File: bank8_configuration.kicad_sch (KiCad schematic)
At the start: 19 parts, among them IC1 ECP5-BGA256, U7 W25Q32JVSS

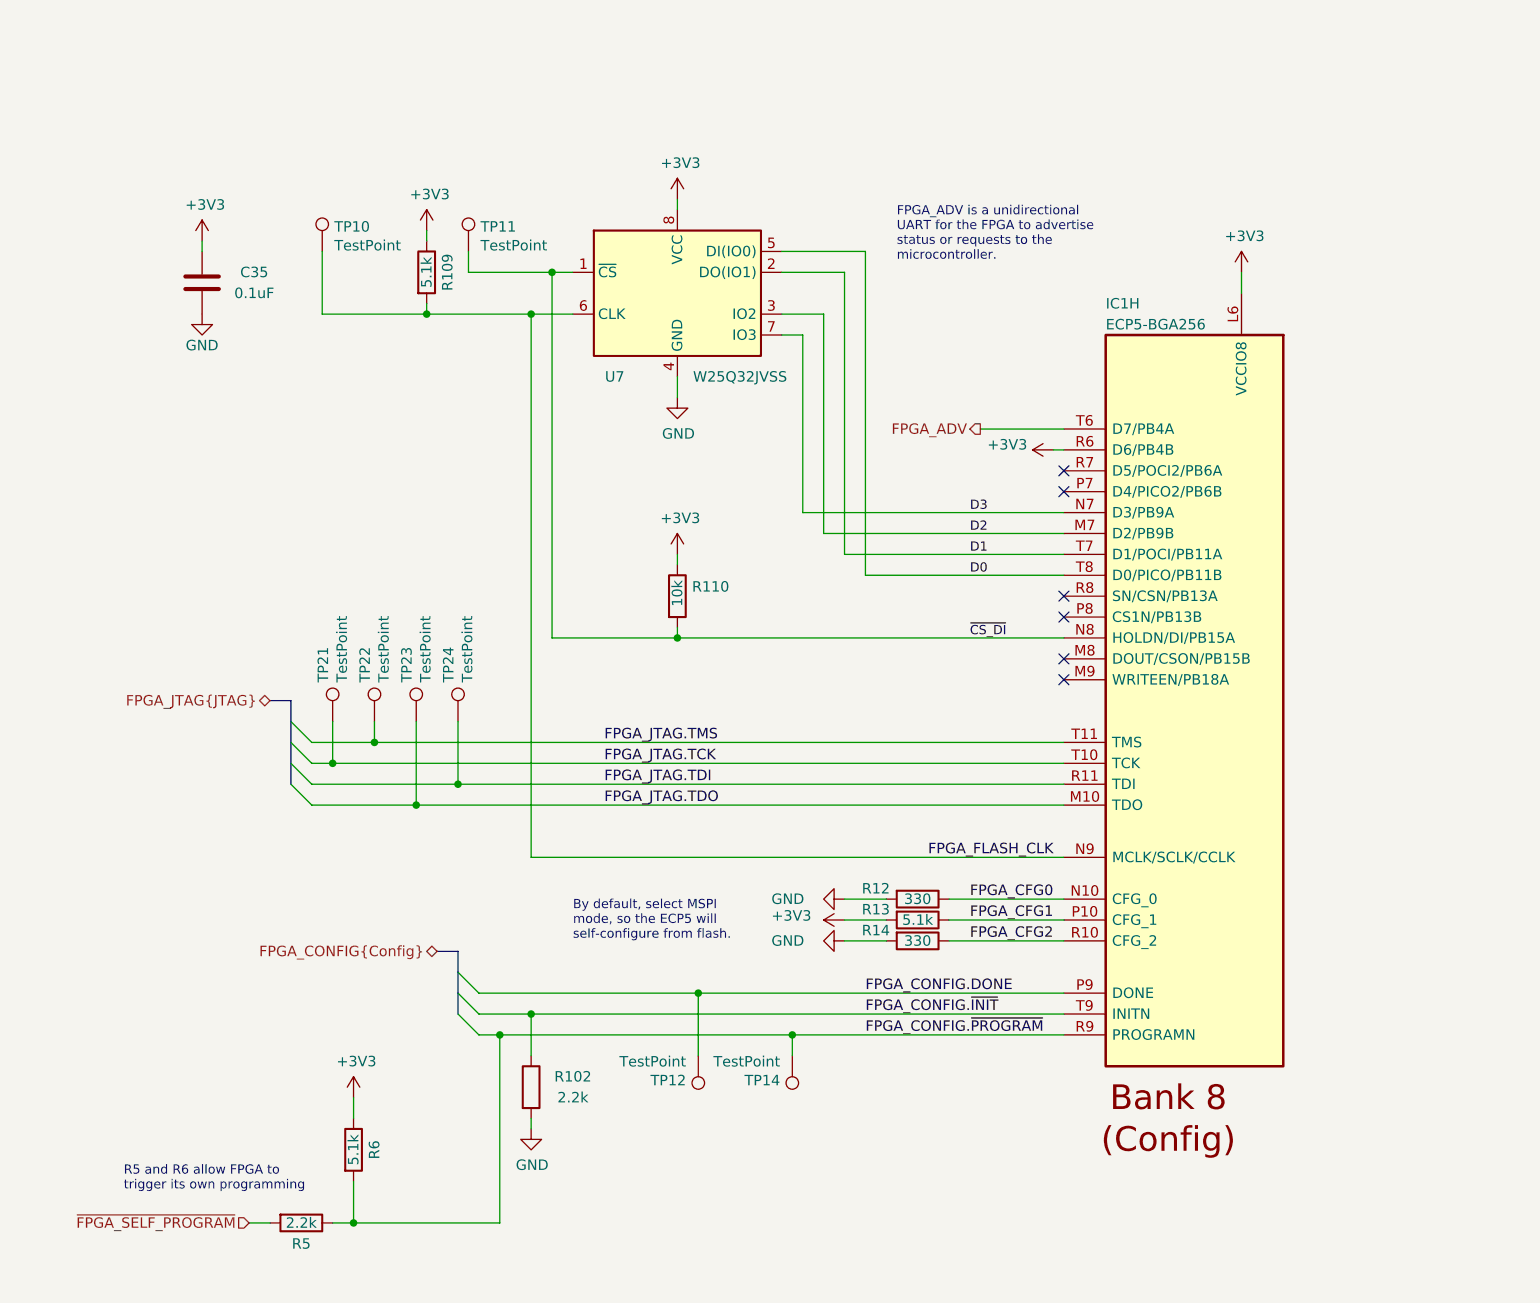
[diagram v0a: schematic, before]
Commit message: Upgrade to KiCad 7
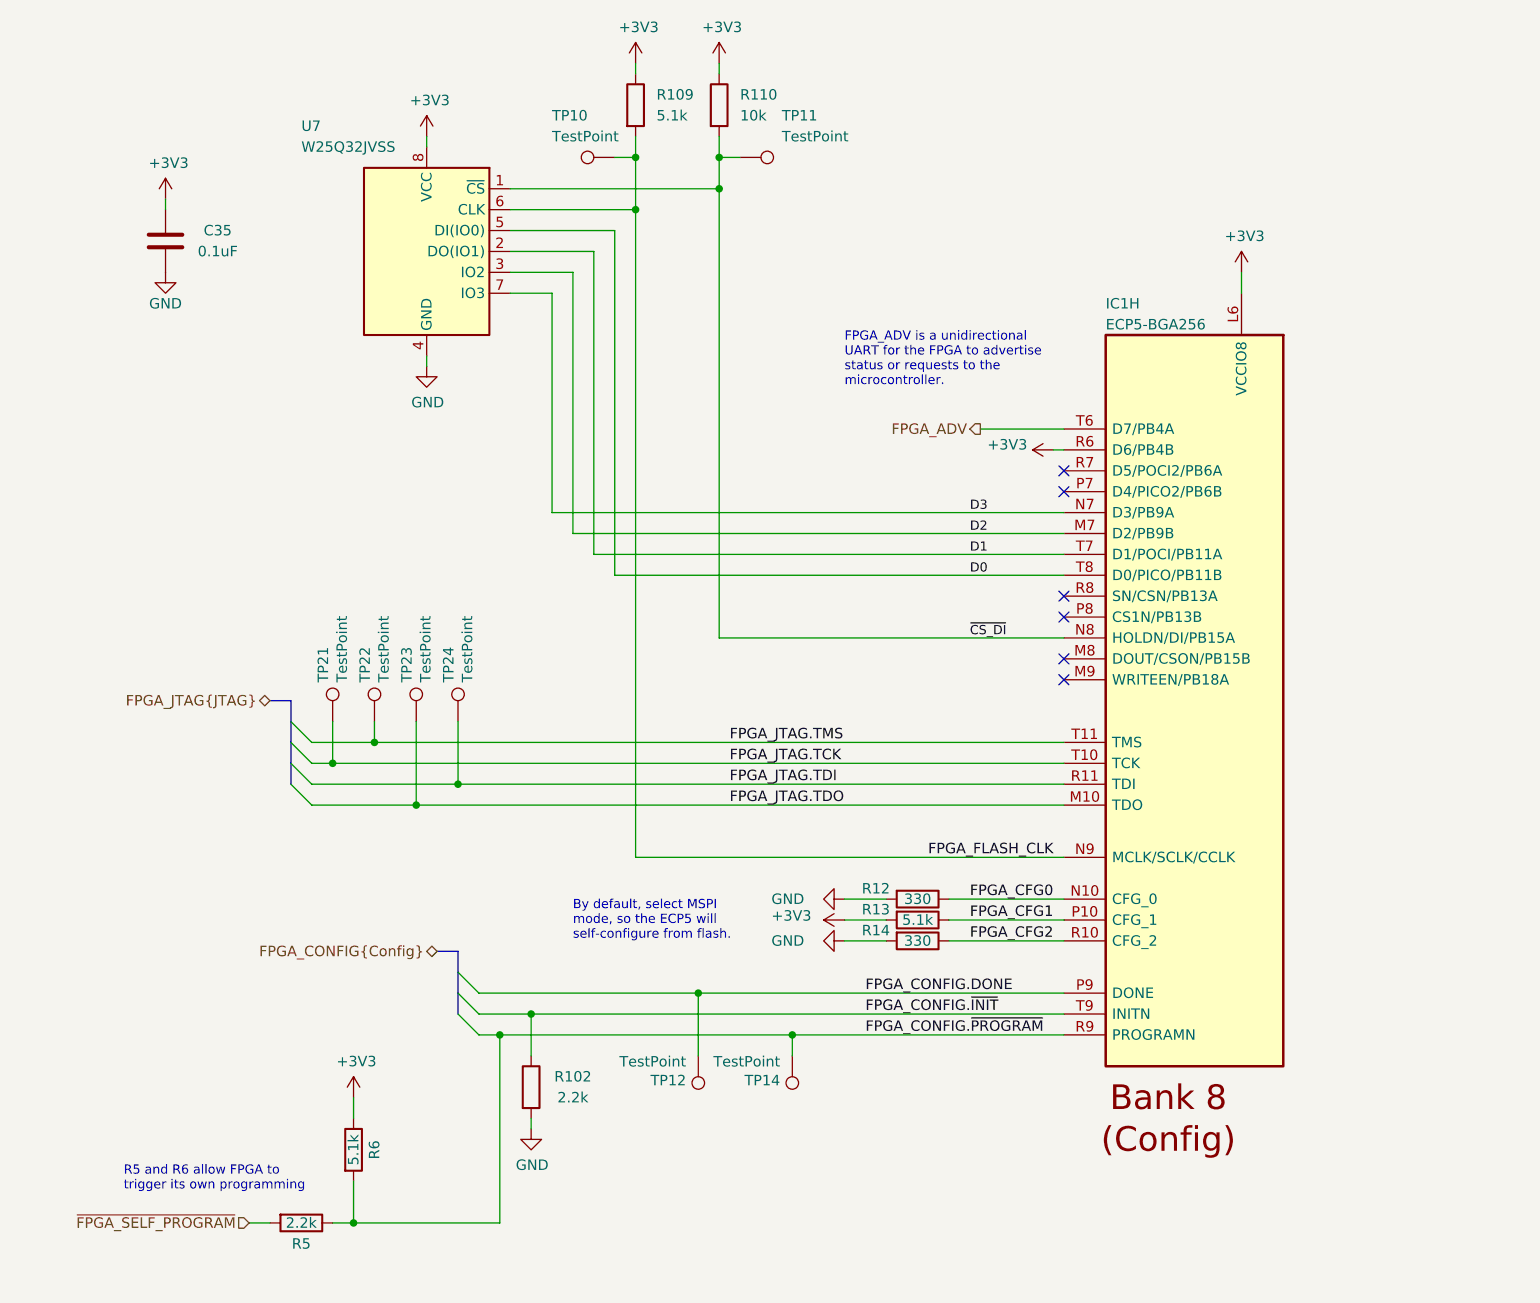
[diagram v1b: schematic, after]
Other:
- moved on the sheet: C35, R109, R110, TP10, TP11, U7

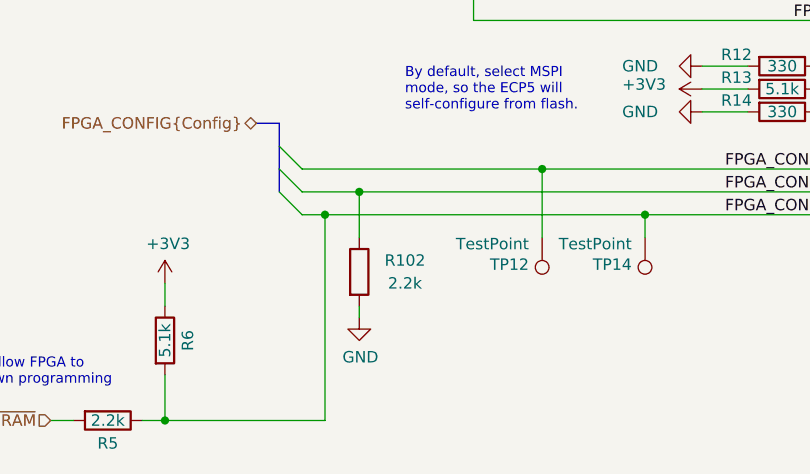
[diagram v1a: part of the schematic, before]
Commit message: Add FPGA_INIT (INITN) series resistor
Fixes #14
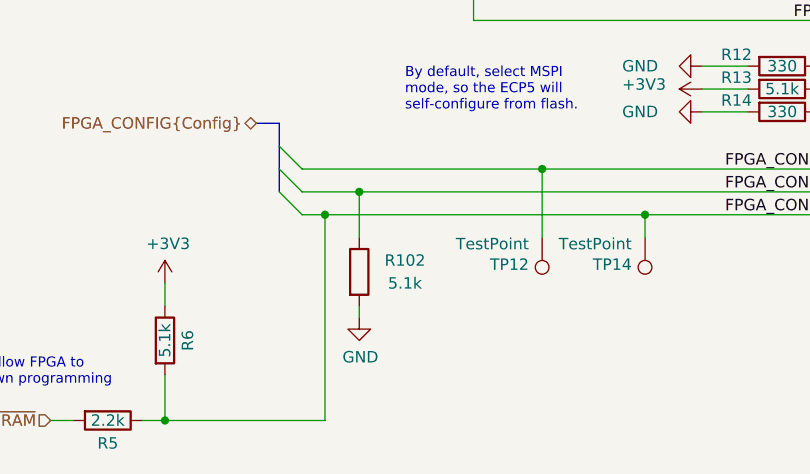
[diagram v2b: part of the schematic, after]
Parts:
- R102: value 2.2k -> 5.1k; Part Number RC0402JR-072K2L -> RC0402JR-075K1L; Substitution any equivalent -> 5.1k
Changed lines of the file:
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@@
       (effects (font (size 1.27 1.27)))
     )
-    (property "Value" "2.2k" (at 116.84 148.59 0)
+    (property "Value" "5.1k" (at 116.84 148.59 0)
       (effects (font (size 1.27 1.27)))
     )
@@
       (effects (font (size 1.27 1.27)) hide)
     )
-    (property "Part Number" "RC0402JR-072K2L" (at 111.76 147.32 0)
+    (property "Part Number" "RC0402JR-075K1L" (at 111.76 147.32 0)
       (effects (font (size 1.27 1.27)) hide)
     )
-    (property "Substitution" "any equivalent" (at 111.76 147.32 0)
+    (property "Substitution" "5.1k" (at 111.76 147.32 0)
       (effects (font (size 1.27 1.27)) hide)
     )
-    (property "Description" "RES 2.2K OHM 5% 1/16W 0402" (at 111.76 147.32 0)
+    (property "Description" "RES 5.1K OHM 5% 1/16W 0402" (at 111.76 147.32 0)
       (effects (font (size 1.27 1.27)) hide)
     )
